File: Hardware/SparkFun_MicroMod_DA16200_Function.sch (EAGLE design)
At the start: 35 parts, among them J1 MICROMOD_STANDARD, J2 CORTEX_JTAG_DEBUG, U1 DA16200MOD, U2 CH340E_MSOP10, U3 3.3V

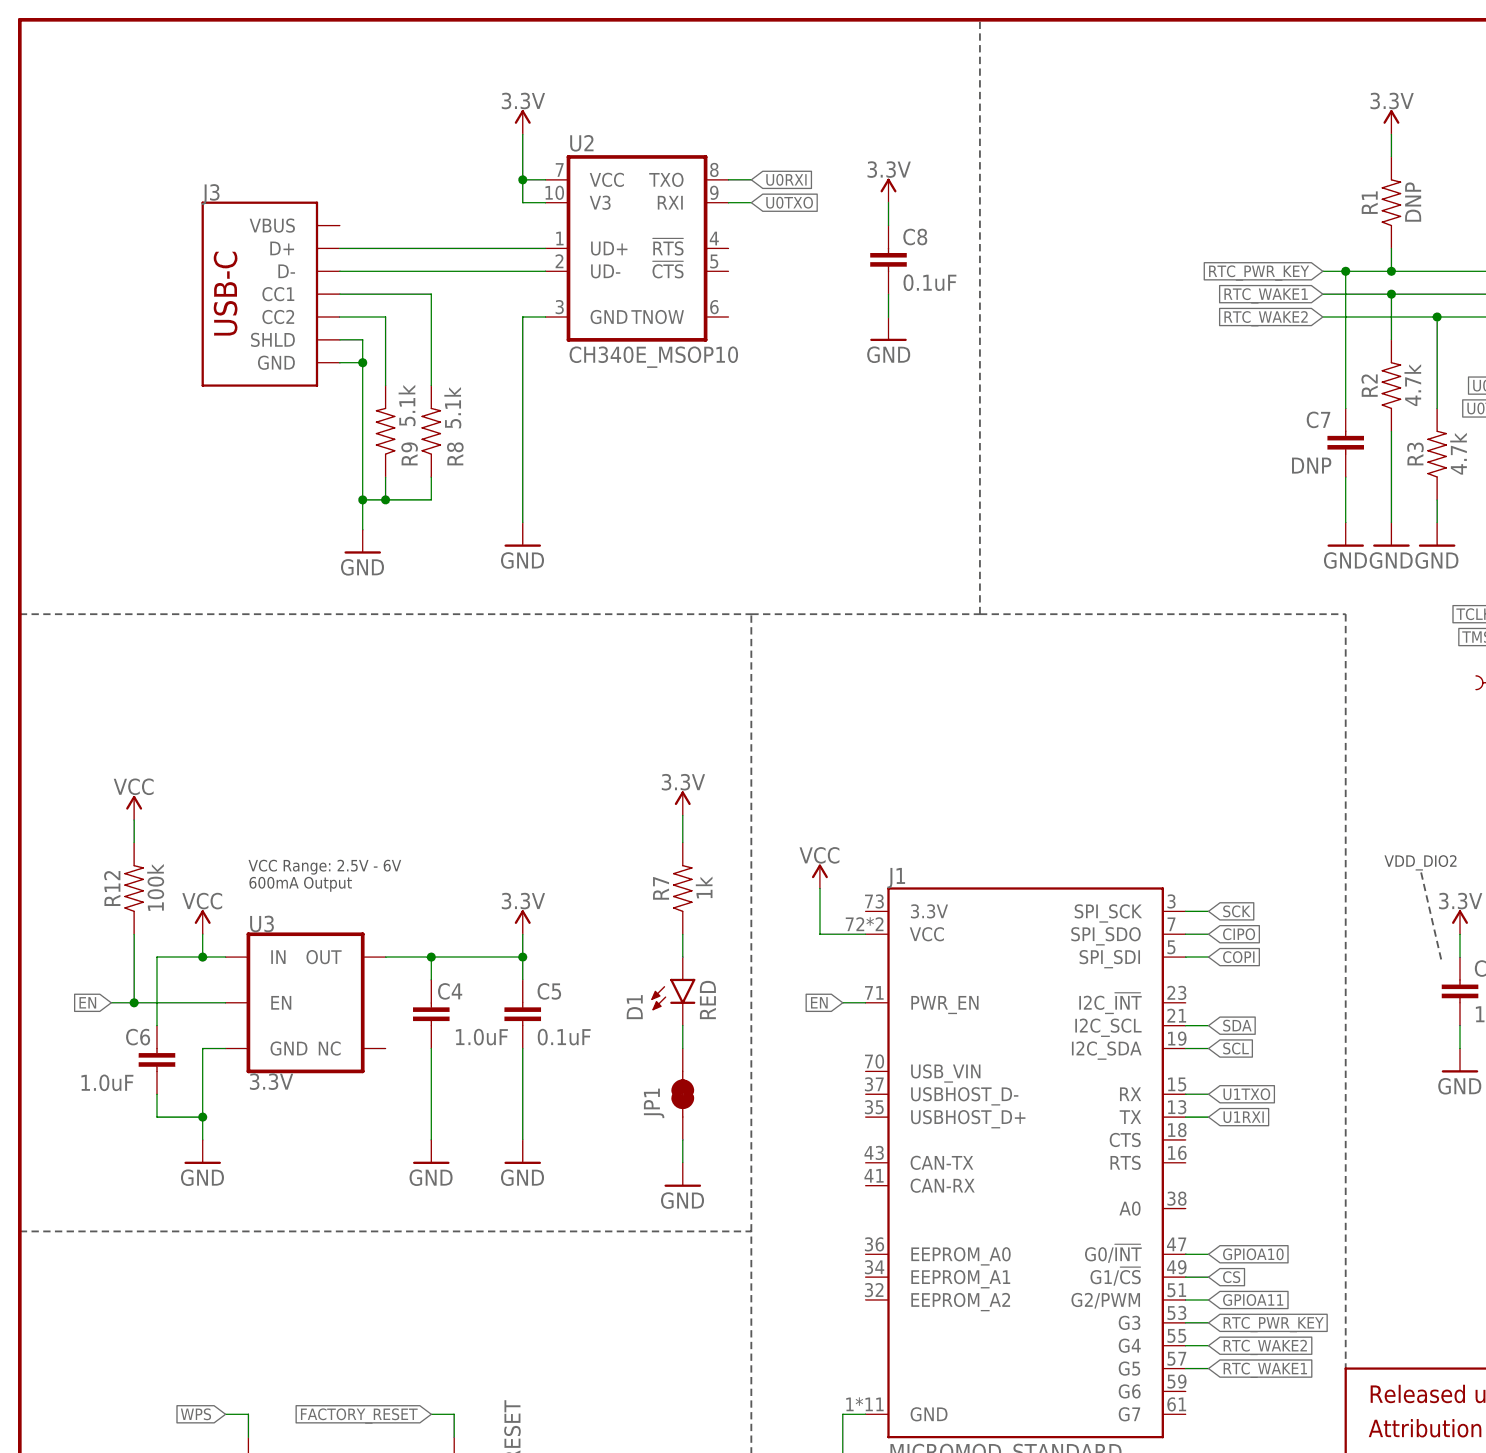
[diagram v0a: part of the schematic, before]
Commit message: Update SparkFun_MicroMod_DA16200_Function.sch
Added labels
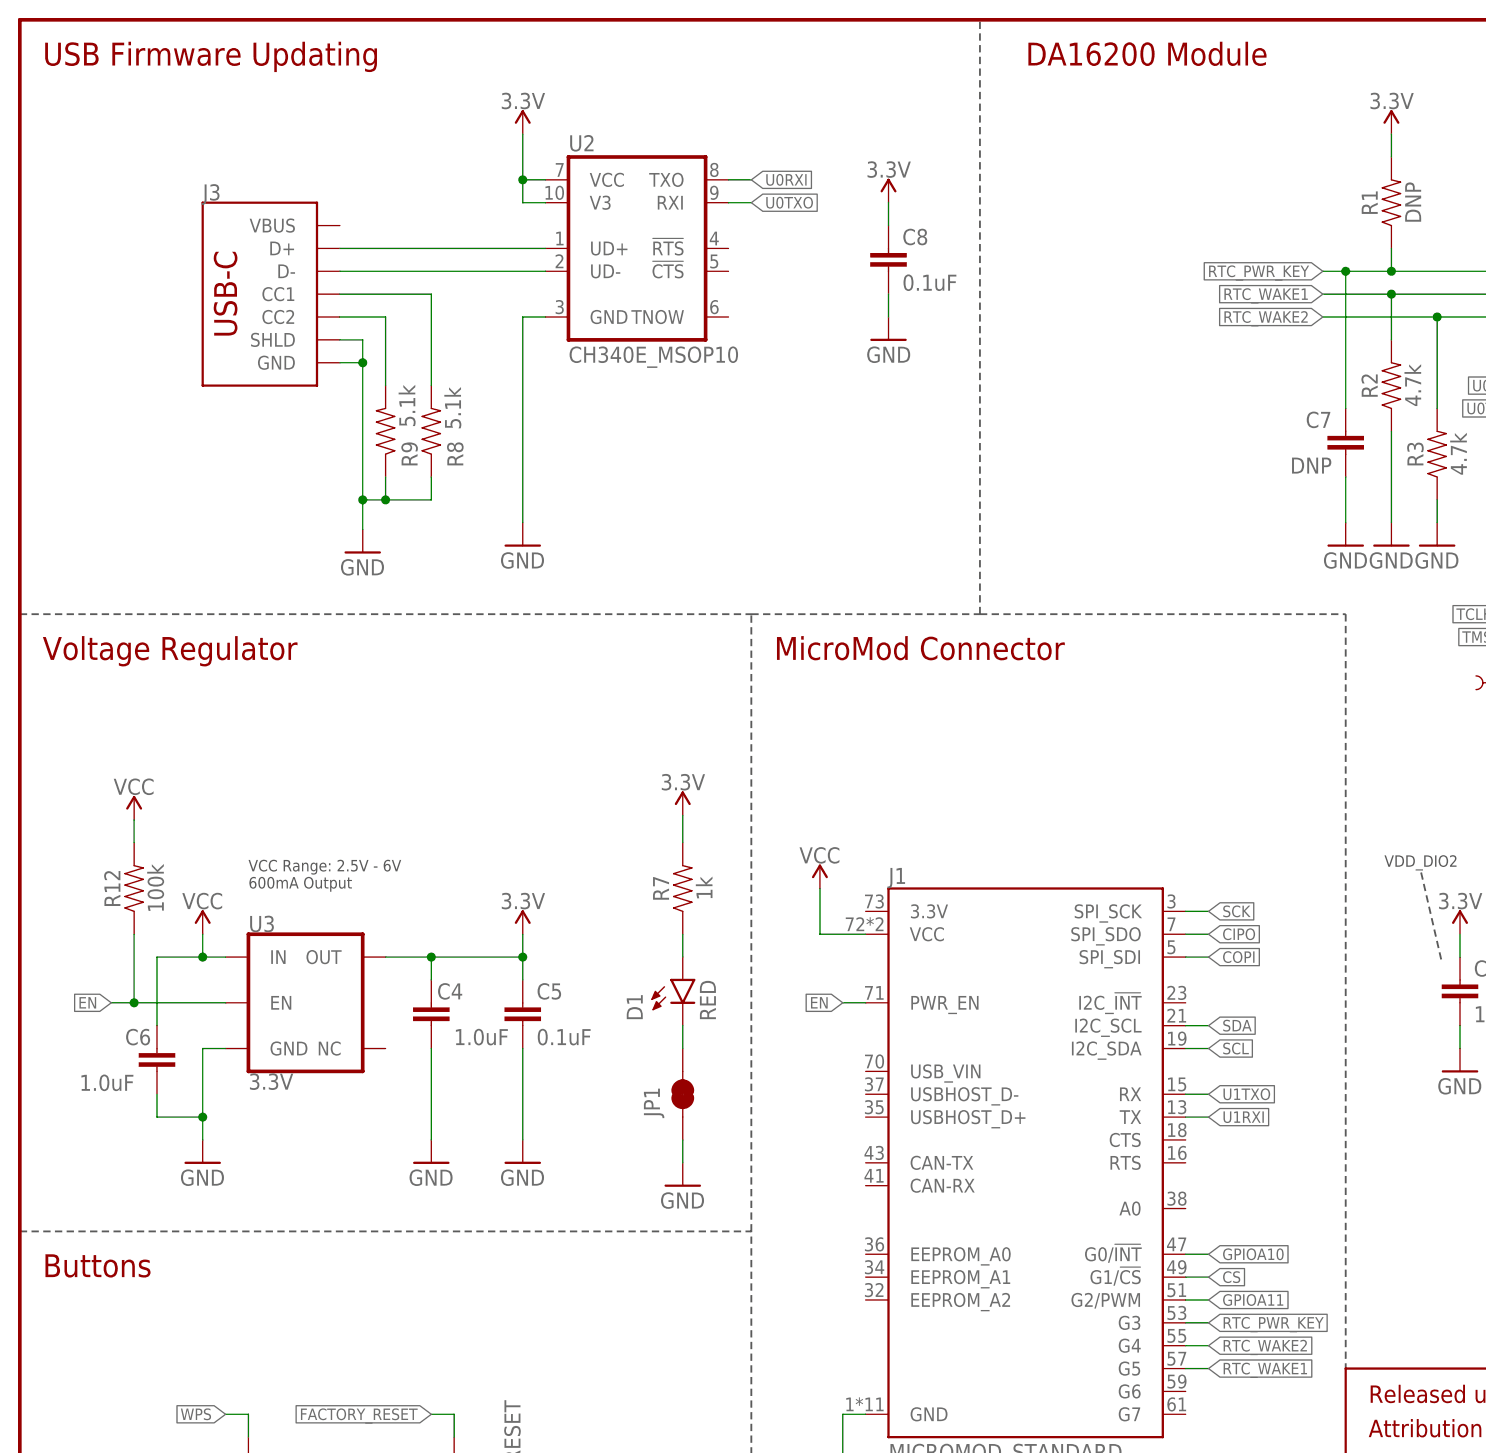
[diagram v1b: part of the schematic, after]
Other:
- note added: "Buttons"
- note added: "DA16200 Module"
- note added: "MicroMod Connector"
- note added: "USB Firmware Updating"
- note added: "Voltage Regulator"
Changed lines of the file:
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@@
 <text x="165.354" y="11.684" size="2.54" layer="94" font="vector">Alex Wende</text>
 <text x="238.252" y="7.112" size="2.54" layer="94" font="vector">V01</text>
+<text x="2.54" y="180.34" size="2.54" layer="94" font="vector">USB Firmware Updating</text>
+<text x="111.76" y="180.34" size="2.54" layer="94" font="vector">DA16200 Module</text>
+<text x="83.82" y="114.3" size="2.54" layer="94" font="vector">MicroMod Connector</text>
+<text x="2.54" y="114.3" size="2.54" layer="94" font="vector">Voltage Regulator</text>
+<text x="2.54" y="45.72" size="2.54" layer="94" font="vector">Buttons</text>
 </plain>
 <instances>

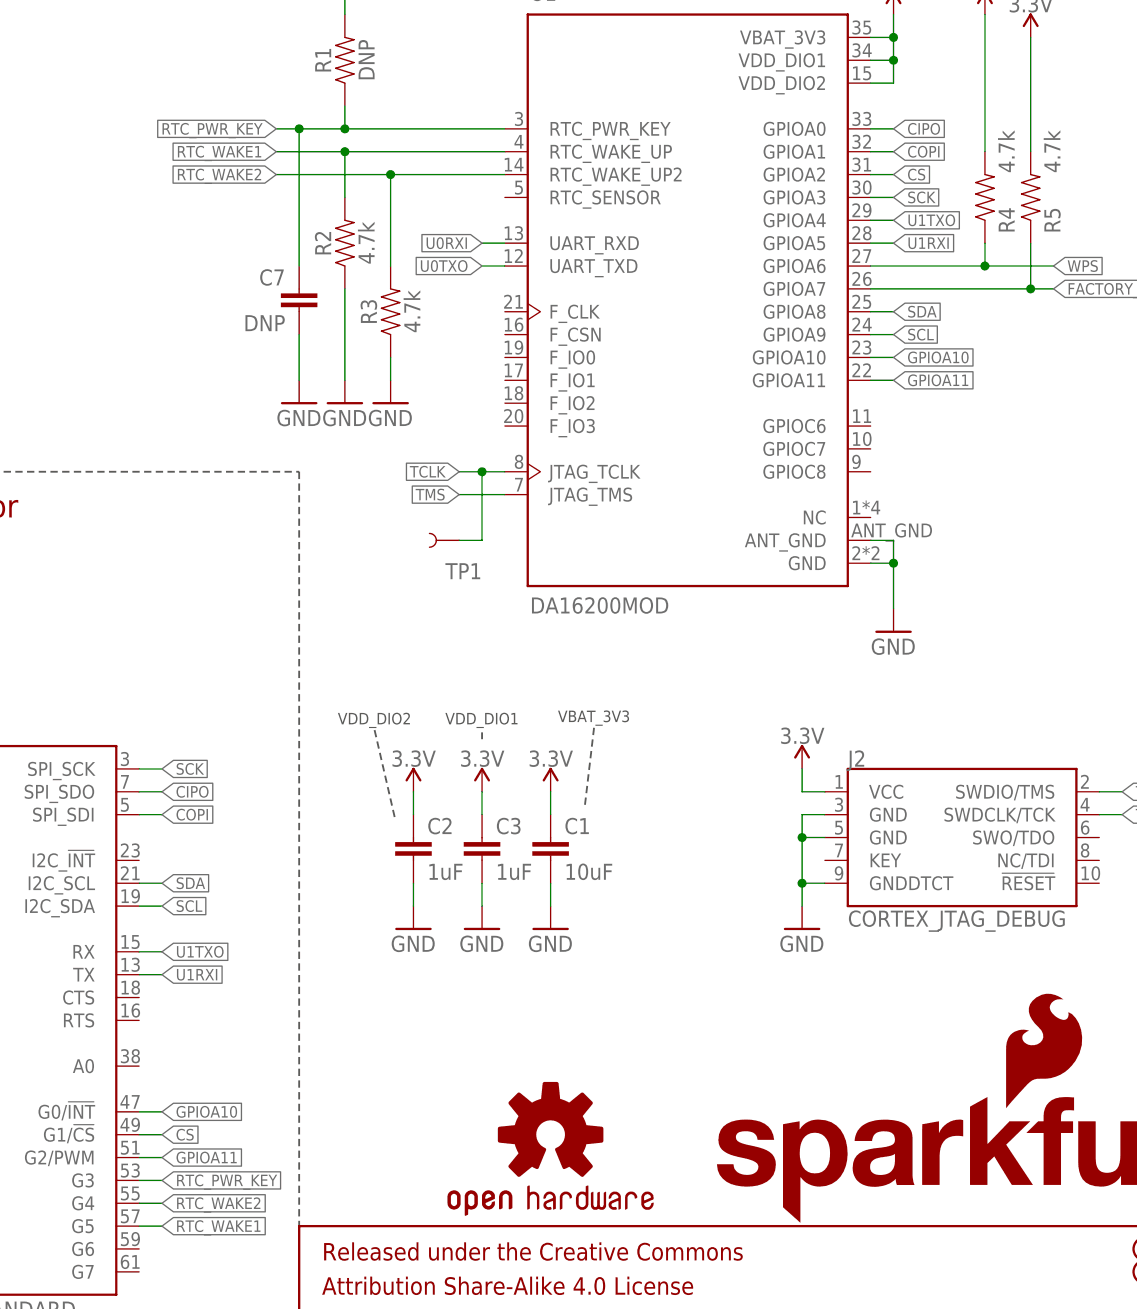
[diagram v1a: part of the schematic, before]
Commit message: Design Review Changes
Swapped U1RX/TX
Corrected SCL/SDA
Added a few more vias on the PCB
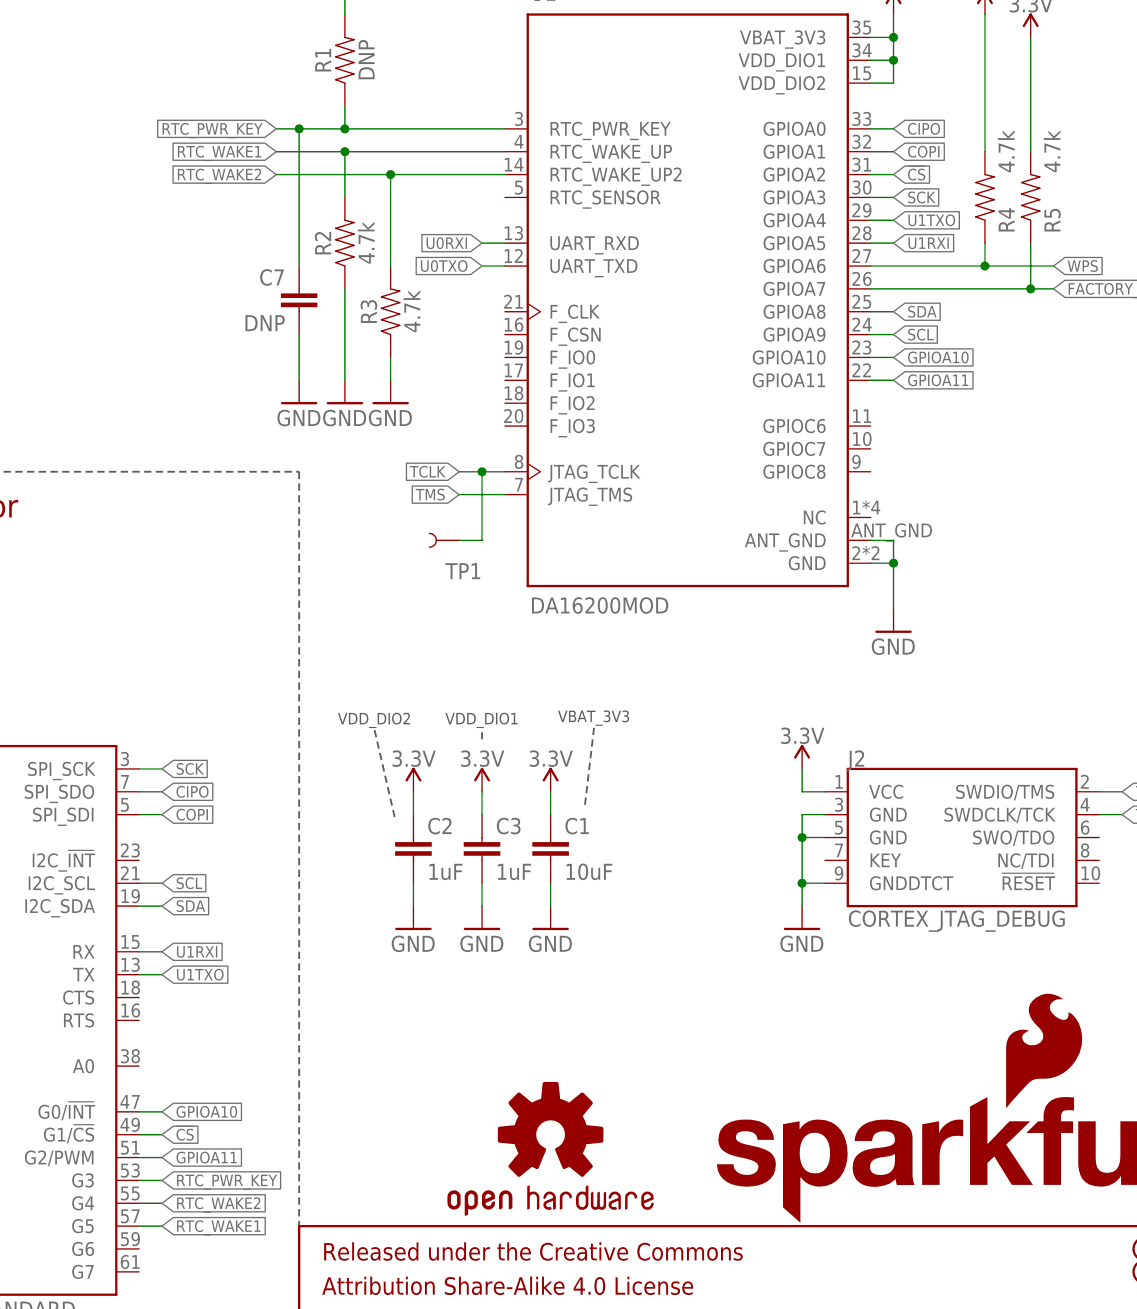
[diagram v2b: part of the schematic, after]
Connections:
- net CS renamed !CS!
- net SCL: now also J1.I2C_SCL; no longer J1.I2C_SDA
- net SDA: now also J1.I2C_SDA; no longer J1.I2C_SCL
- net U1RXI: now also J1.RX; no longer J1.TX
- net U1TXO: now also J1.TX; no longer J1.RX
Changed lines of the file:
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@@
 </segment>
 <segment>
-<pinref part="J1" gate="J1" pin="TX"/>
-<wire x1="129.54" y1="63.5" x2="132.08" y2="63.5" width="0.1524" layer="91"/>
-<label x="132.08" y="63.5" size="1.27" layer="95" xref="yes"/>
+<pinref part="J1" gate="J1" pin="RX"/>
+<wire x1="129.54" y1="66.04" x2="132.08" y2="66.04" width="0.1524" layer="91"/>
+<label x="132.08" y="66.04" size="1.27" layer="95" xref="yes"/>
 </segment>
 </net>
@@
 </segment>
 <segment>
-<pinref part="J1" gate="J1" pin="RX"/>
-<wire x1="129.54" y1="66.04" x2="132.08" y2="66.04" width="0.1524" layer="91"/>
-<label x="132.08" y="66.04" size="1.27" layer="95" xref="yes"/>
+<pinref part="J1" gate="J1" pin="TX"/>
+<wire x1="129.54" y1="63.5" x2="132.08" y2="63.5" width="0.1524" layer="91"/>
+<label x="132.08" y="63.5" size="1.27" layer="95" xref="yes"/>
 </segment>
 </net>
@@
 <net name="SDA" class="0">
 <segment>
-<pinref part="J1" gate="J1" pin="I2C_SCL"/>
-<wire x1="129.54" y1="73.66" x2="132.08" y2="73.66" width="0.1524" layer="91"/>
-<label x="132.08" y="73.66" size="1.27" layer="95" xref="yes"/>
-</segment>
-<segment>
 <pinref part="U1" gate="G$1" pin="GPIOA8"/>
 <wire x1="210.82" y1="137.16" x2="213.36" y2="137.16" width="0.1524" layer="91"/>
 <label x="213.36" y="137.16" size="1.27" layer="95" xref="yes"/>
 </segment>
-</net>
-<net name="SCL" class="0">
 <segment>
 <pinref part="J1" gate="J1" pin="I2C_SDA"/>
@@
 <label x="132.08" y="71.12" size="1.27" layer="95" xref="yes"/>
 </segment>
+</net>
+<net name="SCL" class="0">
 <segment>
 <pinref part="U1" gate="G$1" pin="GPIOA9"/>
 <wire x1="210.82" y1="134.62" x2="213.36" y2="134.62" width="0.1524" layer="91"/>
 <label x="213.36" y="134.62" size="1.27" layer="95" xref="yes"/>
+</segment>
+<segment>
+<pinref part="J1" gate="J1" pin="I2C_SCL"/>
+<wire x1="129.54" y1="73.66" x2="132.08" y2="73.66" width="0.1524" layer="91"/>
+<label x="132.08" y="73.66" size="1.27" layer="95" xref="yes"/>
 </segment>
 </net>
@@
 </segment>
 </net>
-<net name="CS" class="0">
+<net name="!CS!" class="0">
 <segment>
 <pinref part="U1" gate="G$1" pin="GPIOA2"/>

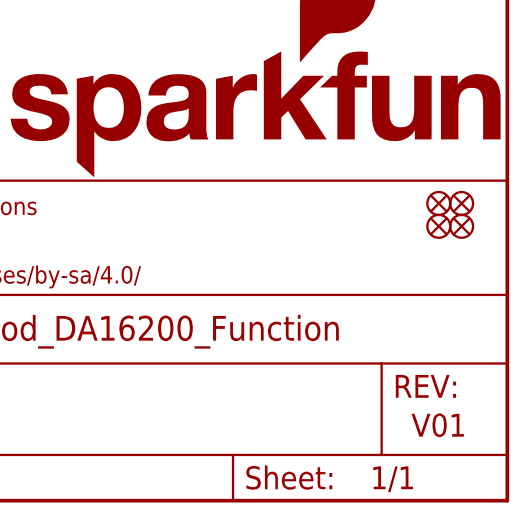
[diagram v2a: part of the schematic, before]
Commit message: Added Ordering Instructions
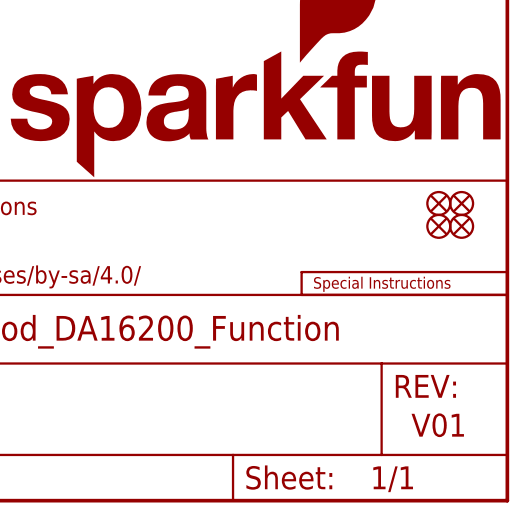
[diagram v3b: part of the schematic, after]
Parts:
- added LOGO3: SPECIAL_INSTRUCTIONS-ORDERING, SparkFun-Aesthetics:SPECIAL_INSTRUCTIONS-ORDERING
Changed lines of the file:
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@@
 <part name="C4" library="SparkFun-Capacitors" deviceset="1.0UF" device="-0603-16V-10%" value="1.0uF"/>
 <part name="C5" library="SparkFun-Capacitors" deviceset="0.1UF" device="-0603-25V-(+80/-20%)" value="0.1uF"/>
+<part name="LOGO3" library="SparkFun-Aesthetics" deviceset="SPECIAL_INSTRUCTIONS" device="-ORDERING"/>
 </parts>
 <sheets>
@@
 <attribute name="VALUE" x="57.404" y="71.501" size="1.778" layer="96" font="vector"/>
 </instance>
+<instance part="LOGO3" gate="G$1" x="226.06" y="22.86" smashed="yes"/>
 </instances>
 <busses>

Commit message: V10
Added EEPROM, I2C Pullups
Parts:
- removed FRAME1: FRAME-LETTER, SparkFun-Aesthetics:FRAME-LETTER
- added C9: 0.1uF, SparkFun-Capacitors:0.1UF-0603-25V-(+80/-20%)
- added FRAME2: FRAME-LEDGER, SparkFun-Aesthetics:FRAME-LEDGER
- added JP2: JUMPER-SMT_3_2-NC_TRACE_SILK, SparkFun-Jumpers:JUMPER-SMT_3_2-NC_TRACE_SILK
- added R10, R6: 4.7k, SparkFun-Resistors:4.7KOHM-0603-1/10W-1%
- added U4: EEPROM, SparkFun-IC-Memory:EEPROM-I2C512K
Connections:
- removed net SCL: J1.I2C_SCL, U1.GPIOA9
- removed net SDA: J1.I2C_SDA, U1.GPIOA8
- new net I2C_SCL: J1.I2C_SCL, R6.1, U1.GPIOA9, U4.SCL
- new net I2C_SDA: J1.I2C_SDA, R10.1, U1.GPIOA8, U4.SDA
- new net N$1: J1.EEPROM_A0, U4.A0
- new net N$13: JP2.1, R10.2
- new net N$14: JP2.3, R6.2
- new net N$8: J1.EEPROM_A2, U4.A2
- new net N$9: J1.EEPROM_A1, U4.A1
- net 3.3V: now also C9.1, JP2.2, U4.VCC
- net GND: now also C9.2, U4.GND, U4.WP
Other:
- note added: "Cut respective jumper to remove I2C data line and/or clock from pullup resistors."
- note added: "Jumpers"
- note added: "M.2 Connector Edge"
- note added: "Power: AP2112"
- note added: "USB-C Firmware Upload"
- note added: "V10"
- note removed: "MicroMod Connector"
- note removed: "USB Firmware Updating"
- note removed: "V01"
- note removed: "Voltage Regulator"
- moved on the sheet: C1, C2, C3, C4, C5, C6, C7, C8, D1, J1, J2, J3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
